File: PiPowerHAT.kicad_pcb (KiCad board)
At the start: 2 copper layers, 65 x 56 mm, 34 parts, among them J1 2444, J3 Conn_01x02, J6 Raspberry_Pi_2_3, J8 2444, Q1 AO3401A, Q2 MMDT5401, Q3 DMG2305UX-13, U1 XL4015

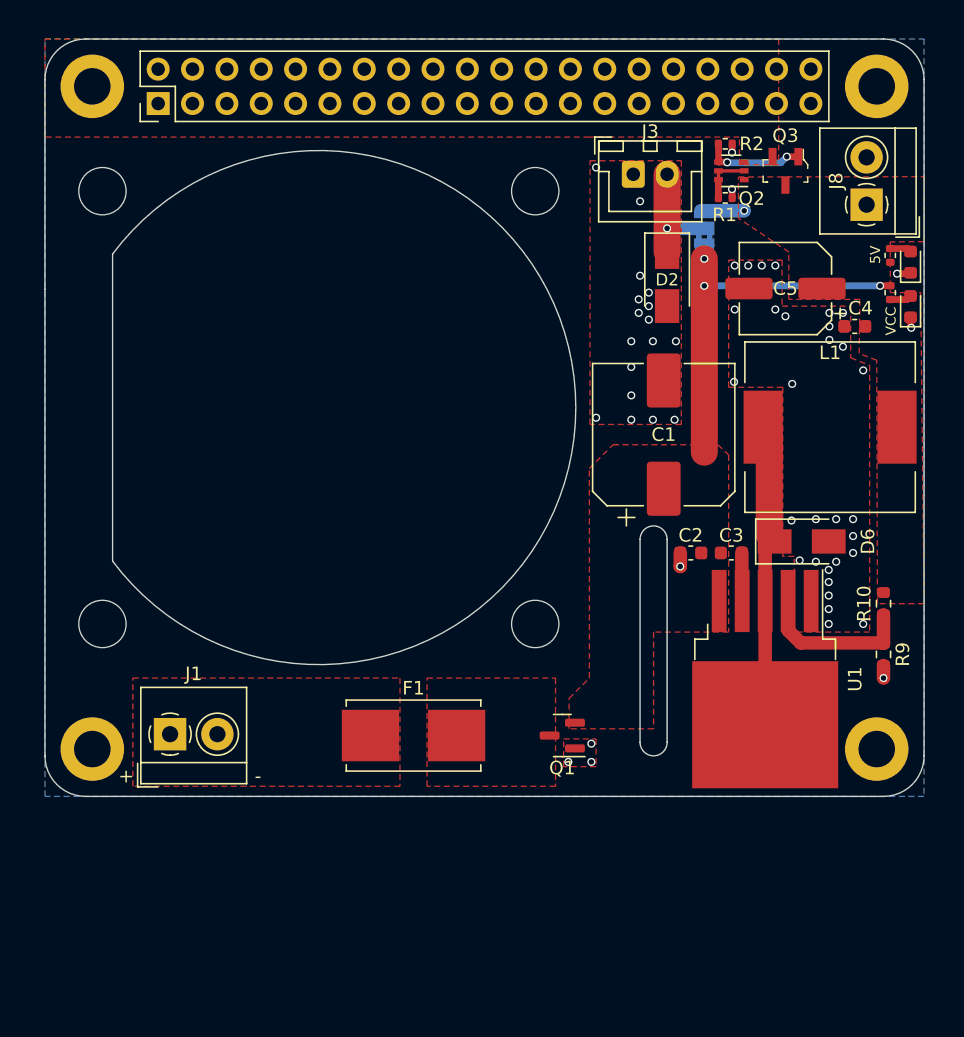
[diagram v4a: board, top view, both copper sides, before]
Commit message: Cleanup and miscellaneous changes. Changed fuseholder and FET
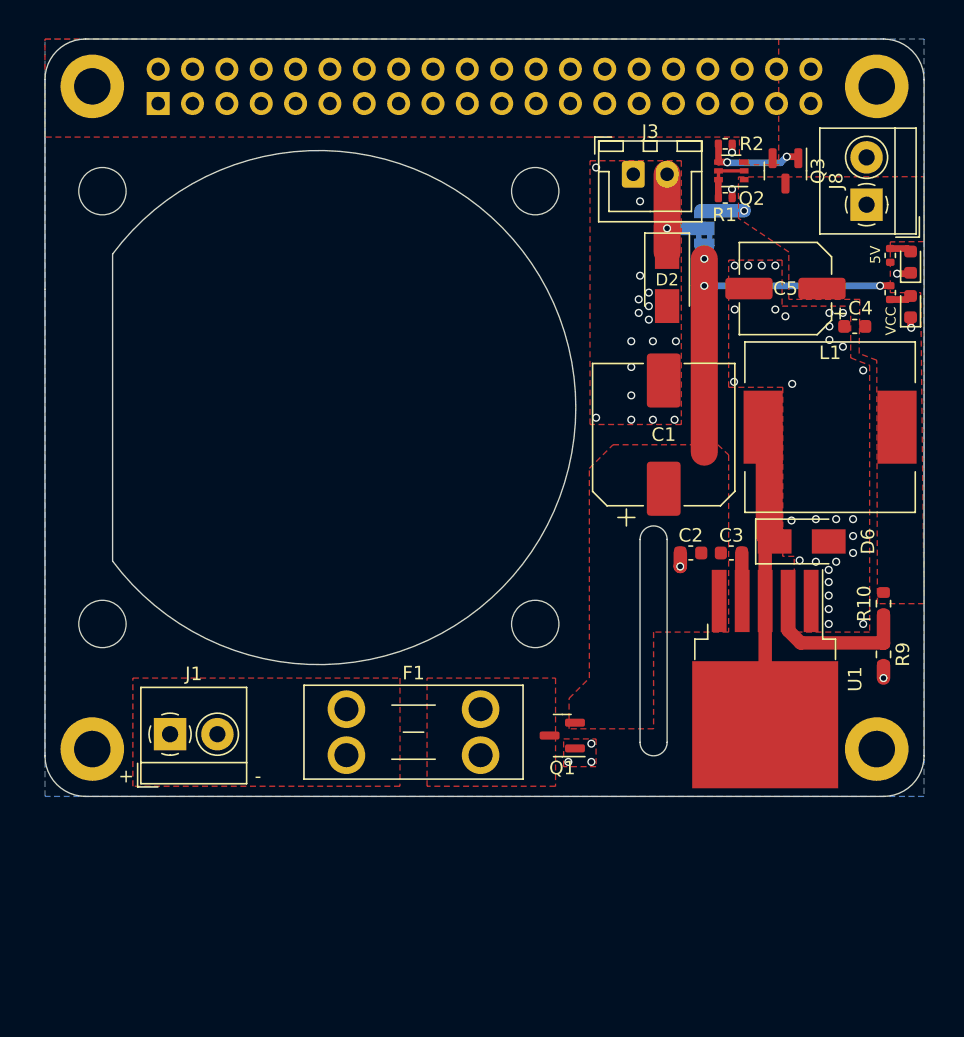
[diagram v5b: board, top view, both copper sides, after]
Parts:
- F1: footprint Fuse:Fuseholder_Littelfuse_Nano2_154x -> Fuse:Fuseholder_Blade_Mini_Keystone_3568
- J6: footprint Connector_PinHeader_2.54mm:PinHeader_2x20_P2.54mm_Vertical -> Connector_PinSocket_2.54mm:PinSocket_2x20_P2.54mm_Vertical; moved to B.Cu
- Q3: value DMG2305UX-13 -> AO3401A; footprint digikey-footprints:SOT-23-3 -> Package_TO_SOT_SMD:SOT-23
- moved F1 5.33 mm to (107.5, 102.8)
- turned J6 to -90 degrees
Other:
- board text added: "JLCJLCJLC"

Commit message: Minor Updates and Cleaning
Changed JLC field to LCSC
Changed Aux power output to JST XH
Small changes to silkscreen labels to hide below components once fitted
Added connector name labels to Frontsilk
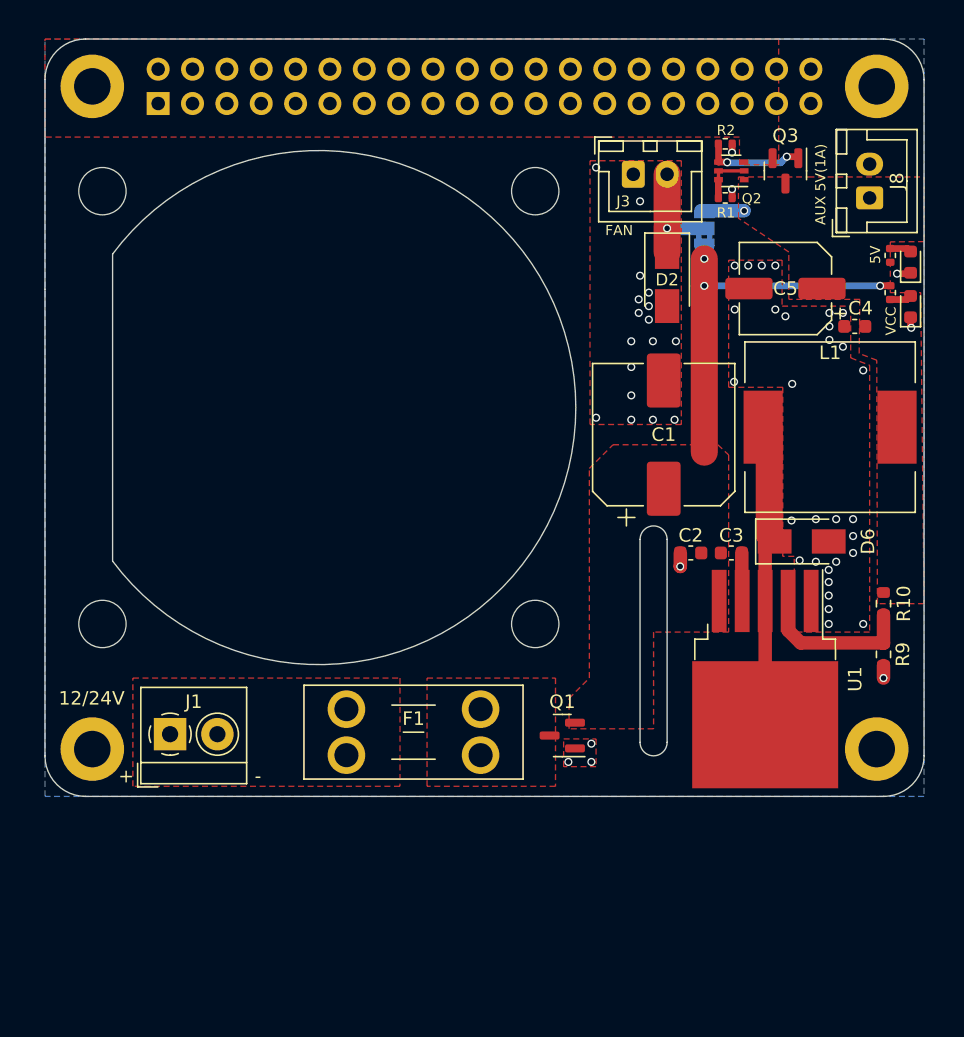
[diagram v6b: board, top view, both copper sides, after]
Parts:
- J8: footprint TerminalBlock_4Ucon:TerminalBlock_4Ucon_1x02_P3.50mm_Horizontal -> Connector_JST:JST_XH_B2B-XH-A_1x02_P2.50mm_Vertical
- moved J8 0.55 mm to (146.2, 65.0)
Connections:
- C2 pad 1: VCC -> unconnected-(C2-Pad1)
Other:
- board text added: "12/24V"
- board text added: "AUX 5V(1A)"
- board text added: "FAN"

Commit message: BOM Updates
Mounting holes and other items not sent to automated manufacture excluded from BOM
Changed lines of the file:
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@@
     (pad_to_mask_clearance 0)
     (pcbplotparams
-      (layerselection 0x0000030_80000001)
+      (layerselection 0x00010bc_ffffffff)
       (disableapertmacros false)
       (usegerberextensions false)
@@
     (property "Sheetfile" "PiPowerHAT.kicad_sch")
     (property "Sheetname" "")
-    (attr through_hole)
+    (property "exclude_from_bom" "")
+    (attr through_hole exclude_from_bom)
     (fp_text reference "J8" (at 1.25 2.025 90) (layer "F.SilkS")
       (effects (font (size 1 1) (thickness 0.15)))
@@
     (fp_line (start 0 -1.35) (end 0.625 -2.35) (layer "F.Fab") (width 0.1))
     (fp_line (start 4.95 3.4) (end 4.95 -2.35) (layer "F.Fab") (width 0.1))
-    (pad "1" thru_hole roundrect (at 0 0 90) (size 1.7 2) (drill 1) (layers *.Cu *.Mask) (roundrect_rratio 0.147059)
+    (pad "1" thru_hole roundrect (at 0 0 90) (size 1.7 2) (drill 1) (layers *.Cu *.Mask) (roundrect_rratio 0.1470588235)
       (net 4 "+5V") (pinfunction "Pin_1") (pintype "passive"))
     (pad "2" thru_hole oval (at 2.5 0 90) (size 1.7 2) (drill 1) (layers *.Cu *.Mask)
@@
     (property "Sheetfile" "PiPowerHAT.kicad_sch")
     (property "Sheetname" "")
-    (attr exclude_from_pos_files)
+    (property "exclude_from_bom" "")
+    (attr exclude_from_pos_files exclude_from_bom)
     (fp_text reference "H2" (at 0 -3.35) (layer "F.SilkS") hide
       (effects (font (size 1 1) (thickness 0.15)))
@@
     (property "Sheetfile" "PiPowerHAT.kicad_sch")
     (property "Sheetname" "")
-    (attr through_hole)
+    (property "exclude_from_bom" "")
+    (attr through_hole exclude_from_bom)
     (fp_text reference "J1" (at 1.75 -2.4) (layer "F.SilkS")
       (effects (font (size 1 1) (thickness 0.15)))
@@
     (property "Sheetfile" "PiPowerHAT.kicad_sch")
     (property "Sheetname" "")
-    (attr exclude_from_pos_files)
+    (property "exclude_from_bom" "")
+    (attr exclude_from_pos_files exclude_from_bom)
     (fp_text reference "H5" (at 0 -4.5) (layer "F.SilkS") hide
       (effects (font (size 1 1) (thickness 0.15)))
@@
     (property "Sheetfile" "PiPowerHAT.kicad_sch")
     (property "Sheetname" "")
-    (attr through_hole)
+    (property "exclude_from_bom" "")
+    (attr through_hole exclude_from_bom)
     (fp_text reference "J3" (at -0.75 2) (layer "F.SilkS")
       (effects (font (size 0.8 0.8) (thickness 0.15)))
@@
     (fp_line (start 0 -1.35) (end 0.625 -2.35) (layer "F.Fab") (width 0.1))
     (fp_line (start -2.45 3.4) (end 4.95 3.4) (layer "F.Fab") (width 0.1))
-    (pad "1" thru_hole roundrect (at 0 0) (size 1.7 2) (drill 1) (layers *.Cu *.Mask) (roundrect_rratio 0.147059)
+    (pad "1" thru_hole roundrect (at 0 0) (size 1.7 2) (drill 1) (layers *.Cu *.Mask) (roundrect_rratio 0.1470588235)
       (net 2 "GND") (pinfunction "Pin_1") (pintype "passive"))
     (pad "2" thru_hole oval (at 2.5 0) (size 1.7 2) (drill 1) (layers *.Cu *.Mask)
@@
     (property "Sheetfile" "PiPowerHAT.kicad_sch")
     (property "Sheetname" "")
-    (attr exclude_from_pos_files)
+    (property "exclude_from_bom" "")
+    (attr exclude_from_pos_files exclude_from_bom)
     (fp_text reference "H6" (at 0 -4.5) (layer "F.SilkS") hide
       (effects (font (size 1 1) (thickness 0.15)))
@@
     (property "Sheetfile" "PiPowerHAT.kicad_sch")
     (property "Sheetname" "")
-    (attr exclude_from_pos_files)
+    (property "exclude_from_bom" "")
+    (attr exclude_from_pos_files exclude_from_bom)
     (fp_text reference "H3" (at 0 -3.35) (layer "F.SilkS") hide
       (effects (font (size 1 1) (thickness 0.15)))
@@
     (property "Sheetfile" "PiPowerHAT.kicad_sch")
     (property "Sheetname" "")
-    (attr exclude_from_pos_files)
+    (property "exclude_from_bom" "")
+    (attr exclude_from_pos_files exclude_from_bom)
     (fp_text reference "H7" (at 0 -4.5) (layer "F.SilkS") hide
       (effects (font (size 1 1) (thickness 0.15)))
@@
     (property "Sheetfile" "PiPowerHAT.kicad_sch")
     (property "Sheetname" "")
-    (attr exclude_from_pos_files)
+    (property "exclude_from_bom" "")
+    (attr exclude_from_pos_files exclude_from_bom)
     (fp_text reference "H8" (at 0 -4.5) (layer "F.SilkS") hide
       (effects (font (size 1 1) (thickness 0.15)))
@@
     (descr "Choke, SMD, 12x12mm 6mm height")
     (tags "Choke SMD")
-    (property "JLC" "C497913")
+    (property "LCSC" "C497913")
     (property "Sheetfile" "PiPowerHAT.kicad_sch")
     (property "Sheetname" "")
@@
     (property "Sheetfile" "PiPowerHAT.kicad_sch")
     (property "Sheetname" "")
-    (attr exclude_from_pos_files)
+    (property "exclude_from_bom" "")
+    (attr exclude_from_pos_files exclude_from_bom)
     (fp_text reference "H1" (at 0 -3.35) (layer "F.SilkS") hide
       (effects (font (size 1 1) (thickness 0.15)))
@@
     (property "Sheetfile" "PiPowerHAT.kicad_sch")
     (property "Sheetname" "")
-    (attr exclude_from_pos_files)
+    (property "exclude_from_bom" "")
+    (attr exclude_from_pos_files exclude_from_bom)
     (fp_text reference "H4" (at 0 -3.35) (layer "F.SilkS") hide
       (effects (font (size 1 1) (thickness 0.15)))
@@
     (property "Sheetfile" "PiPowerHAT.kicad_sch")
     (property "Sheetname" "")
-    (attr through_hole)
+    (property "exclude_from_bom" "")
+    (attr through_hole exclude_from_bom)
     (fp_text reference "J6" (at 2.28 0.02 90) (layer "B.SilkS")
       (effects (font (size 1 1) (thickness 0.15)) (justify mirror))
@@
     (property "Sheetfile" "PiPowerHAT.kicad_sch")
     (property "Sheetname" "")
-    (attr exclude_from_pos_files)
+    (property "exclude_from_bom" "")
+    (attr exclude_from_pos_files exclude_from_bom)
     (fp_text reference "JP1" (at 0 1.8 90) (layer "B.SilkS")
       (effects (font (size 1 1) (thickness 0.15)) (justify mirror))
